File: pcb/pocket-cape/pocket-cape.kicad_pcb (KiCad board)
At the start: 4 copper layers, 55 x 35 mm, 28 parts, among them J1 PhDiode1, J2 12V, J3 PhDiode2, J4 CONN_01X05, U1 MIC920, U2 74LVC2G14GV, U3 ULN2003A, U4 AP3211, U5 MIC920

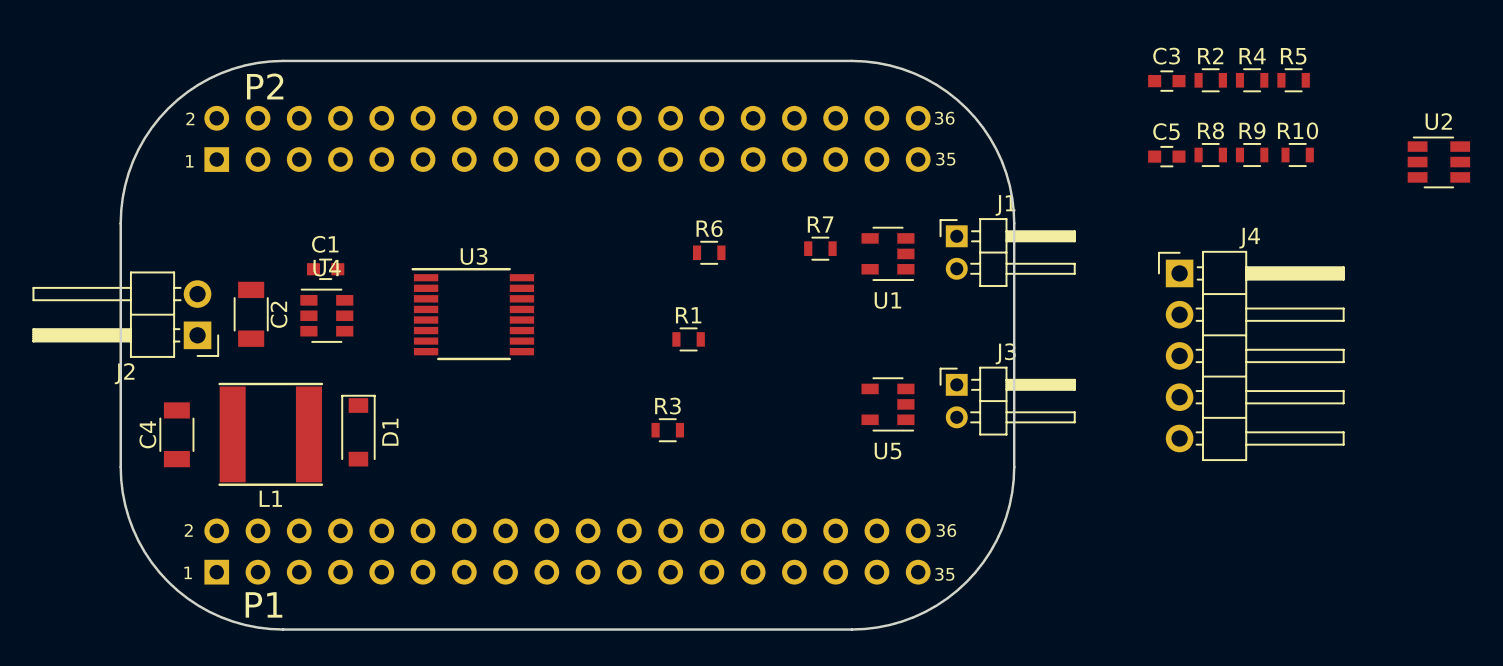
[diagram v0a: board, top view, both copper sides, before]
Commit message: Pocket Cape, pre-routing.
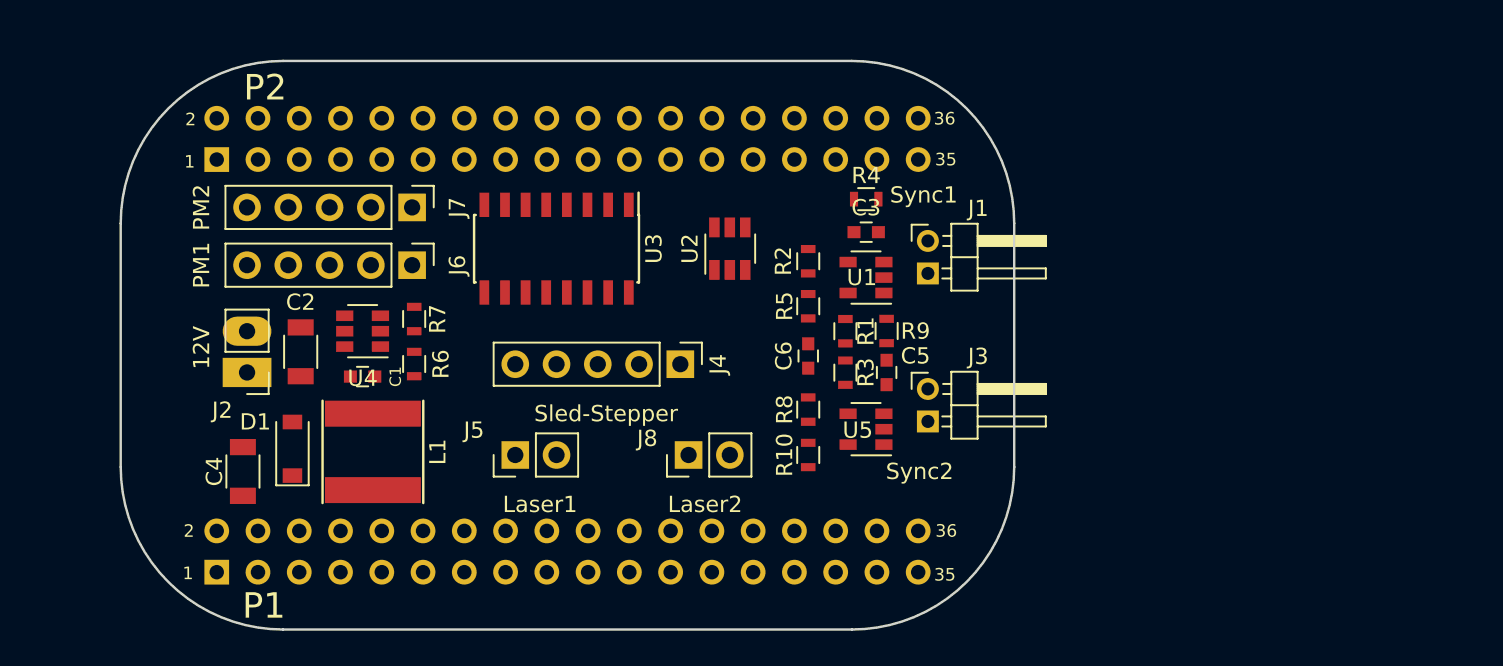
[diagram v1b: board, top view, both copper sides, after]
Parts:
- added C6: 100n, Capacitors_SMD:C_0603, F.Cu at (163.3, 105.7)
- added J5: Laser1, Pin_Headers:Pin_Header_Straight_1x02_Pitch2.54mm, F.Cu at (145.3, 111.8)
- added J6: PM1, Pin_Headers:Pin_Header_Straight_1x05_Pitch2.54mm, F.Cu at (138.9, 100.1)
- added J7: PM2, Pin_Headers:Pin_Header_Straight_1x05_Pitch2.54mm, F.Cu at (138.9, 96.5)
- added J8: Laser2, Pin_Headers:Pin_Header_Straight_1x02_Pitch2.54mm, F.Cu at (156.0, 111.8)
- J1: value PhDiode1 -> Sync1
- J2: footprint Pin_Headers:Pin_Header_Angled_1x02_Pitch2.54mm -> Pin_Headers:Pin_Header_Straight_1x02_Pitch2.54mm
- J3: value PhDiode2 -> Sync2
- J4: value CONN_01X05 -> Sled-Stepper; footprint Pin_Headers:Pin_Header_Angled_1x05_Pitch2.54mm -> Pin_Headers:Pin_Header_Straight_1x05_Pitch2.54mm
- U3: footprint Housings_SSOP:TSSOP-16_4.4x5mm_Pitch0.65mm -> Housings_SOIC:SOIC-16_3.9x9.9mm_Pitch1.27mm
- moved U2 44.0 mm to (158.5, 99.1), turned to 90 degrees
- moved R10 35.3 mm to (163.3, 111.8), turned to 90 degrees
- moved R5 33.0 mm to (163.3, 102.6), turned to 90 degrees
- moved J4 31.2 mm to (155.4, 106.2), turned to 270 degrees
- moved R8 29.3 mm to (163.3, 109.0), turned to 90 degrees
- moved R2 27.2 mm to (163.3, 99.8), turned to 270 degrees
- moved R7 25.4 mm to (139.1, 103.4), turned to 270 degrees
- moved R9 25.0 mm to (168.1, 104.1), turned to 90 degrees
- moved R4 24.9 mm to (166.9, 96.0)
- moved C5 21.8 mm to (168.1, 106.7), turned to 270 degrees
- moved C3 20.7 mm to (166.9, 98.0)
- moved R6 19.4 mm to (139.1, 106.2), turned to 90 degrees
- moved R3 11.5 mm to (165.6, 106.7), turned to 270 degrees
- moved R1 9.67 mm to (165.6, 104.1), turned to 270 degrees
- moved C1 6.98 mm to (135.9, 106.9), turned to 180 degrees
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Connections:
- net Net-(C1-Pad2) renamed /SW
- net Net-(R6-Pad2) renamed /FB
- J1 pad 1: GND -> Net-(C3-Pad2)
- J1 pad 2: Net-(C3-Pad2) -> GND
- J3 pad 1: GND -> Net-(C5-Pad2)
- J3 pad 2: Net-(C5-Pad2) -> GND
- J4 pad 3: GND -> VDD_5V
- P1 pad 20: /(U1.B4)PRU-0.16 -> LASER1
- P1 pad 34: /(U1.R5)GPIO-0.26 -> LASER2
- P2 pad 10: /(U1.R13) -> MIRROR_CLK
- P2 pad 18: /(U1.P7)PRU-0.15 -> STEP4
- P2 pad 22: /(U1.T6)PRU-0.14 -> STEP3
- P2 pad 24: /(U1.P6) -> STEP2
- P2 pad 30: /(U1.B1)PRU-0.3 -> Sync2
- P2 pad 32: /(U1.B2)PRU-0.2 -> Sync1
- P2 pad 33: /(U1.R6) -> STEP1
- P2 pad 4: /(U1.R15) -> ~MIRROR_EN1
- P2 pad 6: /(U1.T15) -> ~MIRROR_EN2
- U2 pad 1: Net-(R2-Pad2) -> Net-(R10-Pad2)
- U2 pad 3: Net-(R10-Pad2) -> Net-(R2-Pad2)
- U2 pad 4: Sync2 -> Sync1
- U2 pad 5: (no net) -> VDD_3V3B
- U2 pad 6: Sync1 -> Sync2
- U3 pad 1: Net-(U3-Pad1) -> STEP1
- U3 pad 10: Net-(U3-Pad10) -> (no net)
- U3 pad 11: Net-(U3-Pad11) -> (no net)
- U3 pad 12: Net-(U3-Pad12) -> (no net)
- U3 pad 2: Net-(U3-Pad2) -> STEP2
- U3 pad 3: Net-(U3-Pad3) -> STEP3
- U3 pad 4: Net-(U3-Pad4) -> STEP4
- U3 pad 5: Net-(U3-Pad5) -> (no net)
- U3 pad 6: Net-(U3-Pad6) -> (no net)
- U3 pad 7: Net-(U3-Pad7) -> (no net)
- U3 pad 8: Net-(U3-Pad8) -> GND
- U3 pad 9: Net-(U3-Pad9) -> GND

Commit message: First rough routing of a PocketBeagle cape.
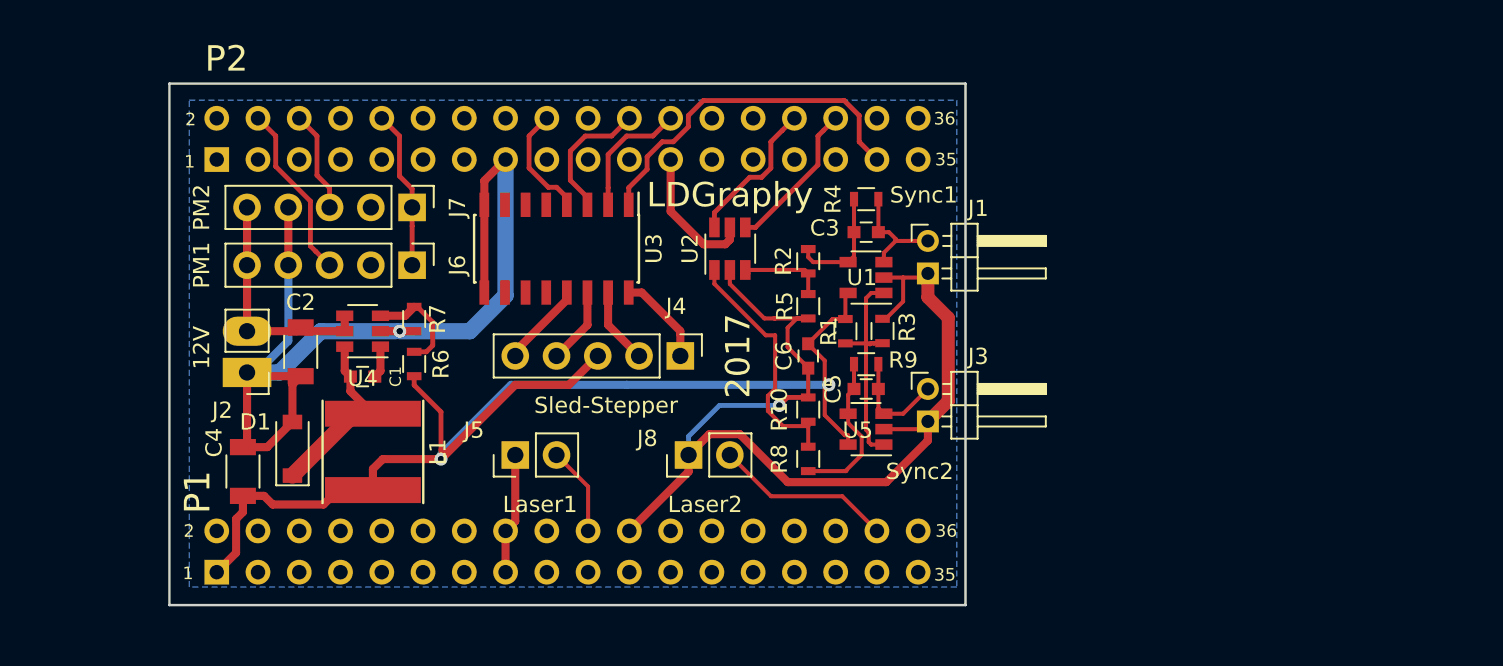
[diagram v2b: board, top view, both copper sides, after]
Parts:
- moved R3 3.44 mm to (167.9, 104.1), turned to 90 degrees
- moved R8 3.04 mm to (163.3, 112.0), turned to 270 degrees
- moved R10 2.79 mm to (163.3, 109.0), turned to 270 degrees
- moved R9 2.40 mm to (166.9, 106.2), turned to 0 degrees
- moved C5 1.62 mm to (166.9, 107.7), turned to 0 degrees
- moved J4 0.51 mm to (155.4, 105.7)
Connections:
- J6 pad 2: Net-(J6-Pad2) -> (no net)
- J7 pad 2: Net-(J7-Pad2) -> (no net)
- P1 pad 10: /(U1.B13)SPI0.MISO -> (no net)
- P1 pad 11: /(U1.L15)USB1.D+ -> (no net)
- P1 pad 12: /(U1.B14)SPI0.MOSI -> (no net)
- P1 pad 13: /(U1.L14)USB1.ID -> (no net)
- P1 pad 14: VDD_3V3B -> Net-(P1-Pad14)
- P1 pad 17: /(U1.B9)VREF- -> (no net)
- P1 pad 18: /(U1.B7)VREF+ -> (no net)
- P1 pad 19: /(U1.A8)AIN0~1.8V -> (no net)
- P1 pad 2: /(U1.F2)AIN6~3.3V -> (no net)
- P1 pad 21: /(U1.B8)AIN1~1.8V -> (no net)
- P1 pad 23: /(U1.B6)AIN2~1.8V -> (no net)
- P1 pad 24: SYS_5V -> Net-(P1-Pad24)
- P1 pad 25: /(U1.C6)AIN3~1.8V -> (no net)
- P1 pad 26: /(U1.B10)I2C2.SDA -> (no net)
- P1 pad 27: /(U1.C7)AIN4~1.8V -> (no net)
- P1 pad 28: /(U1.A10)I2C2.SCL -> (no net)
- P1 pad 29: /(U1.C4)PRU-0.7 -> (no net)
- P1 pad 3: /(U1.M14)USB1.DRVVBUS -> (no net)
- P1 pad 30: /(U1.B12)UART0.TX -> (no net)
- P1 pad 31: /(U1.A3)PRU-0.4 -> (no net)
- P1 pad 32: /(U1.A12)UART0.RX -> (no net)
- P1 pad 33: /(U1.A2)PRU-0.1 -> (no net)
- P1 pad 35: /(U1.F1) -> (no net)
- P1 pad 36: /(U1.A1)PWM0A -> (no net)
- P1 pad 4: /(U1.E1) -> (no net)
- P1 pad 5: /(U1.M15)USB1.VBUS -> (no net)
- P1 pad 6: /(U1.A14)SPI0.CS -> (no net)
- P1 pad 7: USB_DC -> (no net)
- P1 pad 8: /(U1.A13)SPI0.CLK -> (no net)
- P1 pad 9: /(U1.L16)USB1.D- -> (no net)
- P2 pad 1: /(U1.P12)PWM1A -> (no net)
- P2 pad 11: /(U1.A11)I2C1.SDA -> (no net)
- P2 pad 12: /(U1.T11)PWR.BTN -> (no net)
- P2 pad 13: SYS_5V -> (no net)
- P2 pad 14: VIN.BAT -> (no net)
- P2 pad 16: /BAT.TEMP -> (no net)
- P2 pad 17: /(U1.T7) -> (no net)
- P2 pad 19: /(U1.T5) -> (no net)
- P2 pad 2: /(U1.T16) -> (no net)
- P2 pad 20: /(U1.R7) -> (no net)
- P2 pad 25: /(U1.C13)SPI1.MOSI -> (no net)
- P2 pad 26: /(U1.R11)RESET# -> (no net)
- P2 pad 27: /(U1.C12)SPI1.MISO -> (no net)
- P2 pad 28: /(U1.C3)PRU-0.6 -> (no net)
- P2 pad 29: /(U1.C5)SPI1.CLK -> (no net)
- P2 pad 3: /(U1.P5)GPIO-0.23 -> (no net)
- P2 pad 31: /(U1.A4)SPI1.CS -> (no net)
- P2 pad 34: /(U1.B3)PRU-0.5 -> (no net)
- P2 pad 35: /(U1.F3)AIN5~3.3V -> (no net)
- P2 pad 36: /(U1.N13)AIN7~1.8V -> (no net)
- P2 pad 5: /(U1.P15)UART4.RX -> (no net)
- P2 pad 7: /(U1.R16)UART4.TX -> (no net)
- P2 pad 8: /(U1.N14) -> (no net)
- P2 pad 9: /(U1.B11)I2C1.SCL -> (no net)
- U3 pad 10: (no net) -> Net-(U3-Pad10)
- U3 pad 11: (no net) -> Net-(U3-Pad11)
- U3 pad 12: (no net) -> Net-(U3-Pad12)
- U3 pad 5: (no net) -> Net-(U3-Pad5)
- U3 pad 6: (no net) -> Net-(U3-Pad6)
- U3 pad 7: (no net) -> Net-(U3-Pad7)
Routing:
- net GND: track 0.00 -> 137.8 mm, vias 0 -> 2
- net VDD_5V: track 0.00 -> 75.9 mm, vias 0 -> 2
- net STEP1: track 0.00 -> 21.9 mm
- net Net-(R10-Pad2): track 0.00 -> 15.4 mm
- net +12V: track 0.00 -> 14.8 mm
- net /PhotoBias: track 0.00 -> 14.0 mm
- net /SW: track 0.00 -> 11.4 mm
- net LASER2: track 0.00 -> 11.0 mm
- net ~MIRROR_EN1: track 0.00 -> 10.9 mm
- net Net-(C5-Pad1): track 0.00 -> 10.1 mm
- net MIRROR_CLK: track 0.00 -> 9.82 mm
- net Sync1: track 0.00 -> 9.39 mm
- net Sync2: track 0.00 -> 9.19 mm
- net VDD_3V3B: track 0.00 -> 8.55 mm
- net STEP3: track 0.00 -> 8.21 mm
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- added copper zone on B.Cu, net GND
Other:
- board size 55 x 35 mm -> 49 x 32.1 mm
- net class Default: clearance 0 -> 0.18
- rule trace_clearance: 0 -> 0.18
- board text added: "%%gitversion%%"
- board text added: "2017"
- board text added: "LDGraphy"
- board text added: "github.com/hzeller/ldgraphy"

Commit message: Make vias larger for easier home-fabbing.
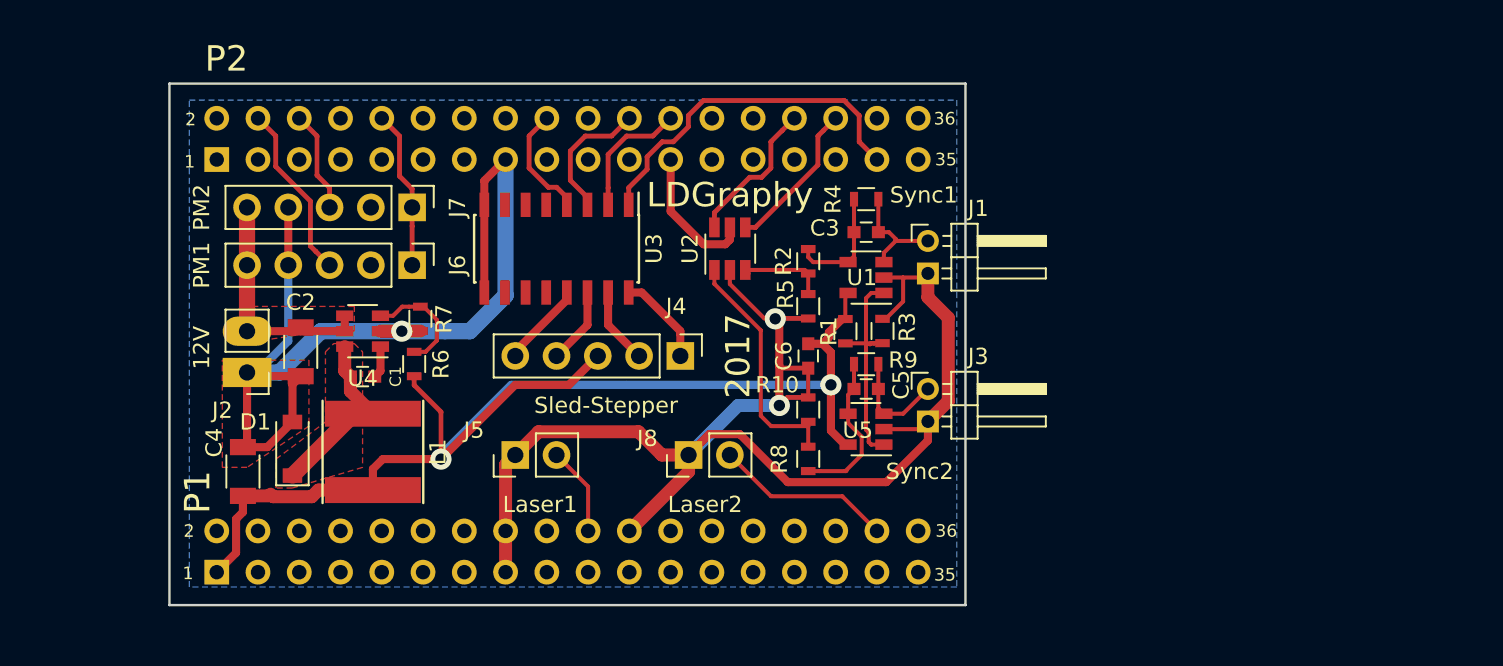
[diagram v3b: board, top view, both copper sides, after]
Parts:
- moved R7 0.38 mm to (139.4, 103.4)
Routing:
- net GND: track 137.8 -> 152.4 mm, vias 2 -> 3
- net VDD_5V: track 75.9 -> 77.4 mm
- added copper zone on F.Cu, net +12V
- added copper zone on F.Cu, net /SW
- added copper zone on F.Cu, net GND
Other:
- net class Default: via_dia 0.8 -> 1.3; via_drill 0.4 -> 0.7
- rule via_min_drill: 0.3 -> 0.7
- rule via_min_size: 0.4 -> 1.3

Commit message: Adjust header distance to accomodate space to use JST XH headers.
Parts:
- added REF***: OSHW-Logo2_9.8x8mm_SilkScreen, Symbols:OSHW-Logo2_9.8x8mm_SilkScreen, B.Cu at (149.4, 98.3)
- J1, J3: footprint Pin_Headers:Pin_Header_Angled_1x02_Pitch2.00mm -> Connectors_JST:JST_PH_S2B-PH-K_02x2.00mm_Angled
- J2, J5, J8: footprint Pin_Headers:Pin_Header_Straight_1x02_Pitch2.54mm -> Connectors_JST:JST_XH_B02B-XH-A_02x2.50mm_Straight
- J4: value Sled-Stepper -> Sled; footprint Pin_Headers:Pin_Header_Straight_1x05_Pitch2.54mm -> Connectors_JST:JST_XH_B05B-XH-A_05x2.50mm_Straight
- moved J3 2.31 mm to (170.6, 110.0), turned to 90 degrees
- moved J1 2.02 mm to (170.6, 100.6), turned to 90 degrees
- moved D1 0.89 mm to (131.4, 112.2)
- moved C2 0.73 mm to (132.8, 105.5)
- moved U3 0.72 mm to (147.3, 98.6)
- moved J2 0.69 mm to (128.1, 106.8), turned to 90 degrees
- moved J4 0.51 mm to (155.4, 106.2), turned to 180 degrees
- moved C4 0.40 mm to (128.4, 112.4)
- moved R6 0.38 mm to (139.4, 106.2)
- turned J5 to 0 degrees
- turned J8 to 0 degrees
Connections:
- J1 pad 1: Net-(C3-Pad2) -> GND
- J1 pad 2: GND -> Net-(C3-Pad2)
- J3 pad 1: Net-(C5-Pad2) -> GND
- J3 pad 2: GND -> Net-(C5-Pad2)
- J6 pad 2: (no net) -> Net-(J6-Pad2)
- J7 pad 2: (no net) -> Net-(J7-Pad2)
- P1 pad 10: (no net) -> /(U1.B13)SPI0.MISO
- P1 pad 11: (no net) -> /(U1.L15)USB1.D+
- P1 pad 12: (no net) -> /(U1.B14)SPI0.MOSI
- P1 pad 13: (no net) -> /(U1.L14)USB1.ID
- P1 pad 14: Net-(P1-Pad14) -> (no net)
- P1 pad 17: (no net) -> /(U1.B9)VREF-
- P1 pad 18: (no net) -> /(U1.B7)VREF+
- P1 pad 19: (no net) -> /(U1.A8)AIN0~1.8V
- P1 pad 2: (no net) -> /(U1.F2)AIN6~3.3V
- P1 pad 21: (no net) -> /(U1.B8)AIN1~1.8V
- P1 pad 23: (no net) -> /(U1.B6)AIN2~1.8V
- P1 pad 24: Net-(P1-Pad24) -> (no net)
- P1 pad 25: (no net) -> /(U1.C6)AIN3~1.8V
- P1 pad 26: (no net) -> /(U1.B10)I2C2.SDA
- P1 pad 27: (no net) -> /(U1.C7)AIN4~1.8V
- P1 pad 28: (no net) -> /(U1.A10)I2C2.SCL
- P1 pad 29: (no net) -> /(U1.C4)PRU-0.7
- P1 pad 3: (no net) -> /(U1.M14)USB1.DRVVBUS
- P1 pad 30: (no net) -> /(U1.B12)UART0.TX
- P1 pad 31: (no net) -> /(U1.A3)PRU-0.4
- P1 pad 32: (no net) -> /(U1.A12)UART0.RX
- P1 pad 33: (no net) -> /(U1.A2)PRU-0.1
- P1 pad 35: (no net) -> /(U1.F1)
- P1 pad 36: (no net) -> /(U1.A1)PWM0A
- P1 pad 4: (no net) -> /(U1.E1)
- P1 pad 5: (no net) -> /(U1.M15)USB1.VBUS
- P1 pad 6: (no net) -> /(U1.A14)SPI0.CS
- P1 pad 7: (no net) -> USB_DC
- P1 pad 8: (no net) -> /(U1.A13)SPI0.CLK
- P1 pad 9: (no net) -> /(U1.L16)USB1.D-
- P2 pad 1: (no net) -> /(U1.P12)PWM1A
- P2 pad 11: (no net) -> /(U1.A11)I2C1.SDA
- P2 pad 12: (no net) -> /(U1.T11)PWR.BTN
- P2 pad 13: (no net) -> SYS_5V
- P2 pad 14: (no net) -> VIN.BAT
- P2 pad 16: (no net) -> /BAT.TEMP
- P2 pad 17: (no net) -> /(U1.T7)
- P2 pad 19: (no net) -> /(U1.T5)
- P2 pad 2: (no net) -> /(U1.T16)
- P2 pad 20: (no net) -> /(U1.R7)
- P2 pad 25: (no net) -> /(U1.C13)SPI1.MOSI
- P2 pad 26: (no net) -> /(U1.R11)RESET#
- P2 pad 27: (no net) -> /(U1.C12)SPI1.MISO
- P2 pad 28: (no net) -> /(U1.C3)PRU-0.6
- P2 pad 29: (no net) -> /(U1.C5)SPI1.CLK
- P2 pad 3: (no net) -> /(U1.P5)GPIO-0.23
- P2 pad 31: (no net) -> /(U1.A4)SPI1.CS
- P2 pad 34: (no net) -> /(U1.B3)PRU-0.5
- P2 pad 35: (no net) -> /(U1.F3)AIN5~3.3V
- P2 pad 36: (no net) -> /(U1.N13)AIN7~1.8V
- P2 pad 5: (no net) -> /(U1.P15)UART4.RX
- P2 pad 7: (no net) -> /(U1.R16)UART4.TX
- P2 pad 8: (no net) -> /(U1.N14)
- P2 pad 9: (no net) -> /(U1.B11)I2C1.SCL
- U3 pad 10: Net-(U3-Pad10) -> (no net)
- U3 pad 11: Net-(U3-Pad11) -> (no net)
- U3 pad 12: Net-(U3-Pad12) -> (no net)
- U3 pad 5: Net-(U3-Pad5) -> (no net)
- U3 pad 6: Net-(U3-Pad6) -> (no net)
- U3 pad 7: Net-(U3-Pad7) -> (no net)
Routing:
- net GND: track 152.4 -> 161.0 mm, vias 3 -> 4
- net VDD_5V: track 77.4 -> 70.0 mm
- net +12V: track 14.8 -> 16.6 mm
- net /SW: track 11.4 -> 13.1 mm
- net Net-(J4-Pad2): track 4.69 -> 5.94 mm
- net Net-(J4-Pad1): track 5.69 -> 6.45 mm
- net Net-(J4-Pad4): track 4.69 -> 5.45 mm
- net Net-(J4-Pad5): track 5.22 -> 5.96 mm
- net /FB: track 7.00 -> 6.30 mm
- net STEP3: track 8.21 -> 8.83 mm
- added copper zone on F.Cu, net VDD_5V
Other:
- net class Default: clearance 0.18 -> 0
- rule trace_clearance: 0.18 -> 0
- board text added: "HZ"
